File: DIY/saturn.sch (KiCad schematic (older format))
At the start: 7 parts, among them J1 Conn_01x09, J2 Conn_01x09, J3 DB25_Male, U1 74AHCT125N, U2 74AHCT125N, U3 74AHCT125N, U4 74AHCT125N

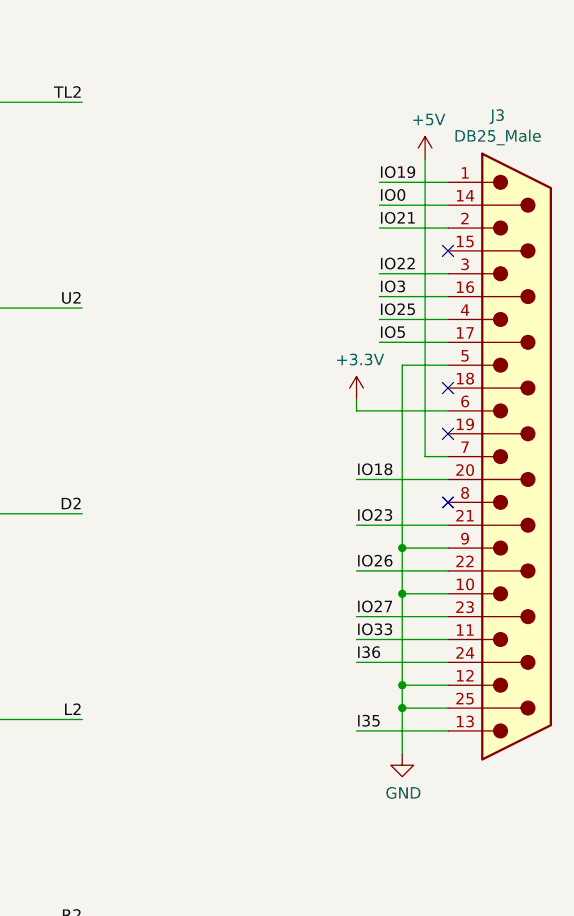
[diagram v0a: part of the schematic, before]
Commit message: [DIY] Update DIY & cable adapter schematic base on new DB25 mapping
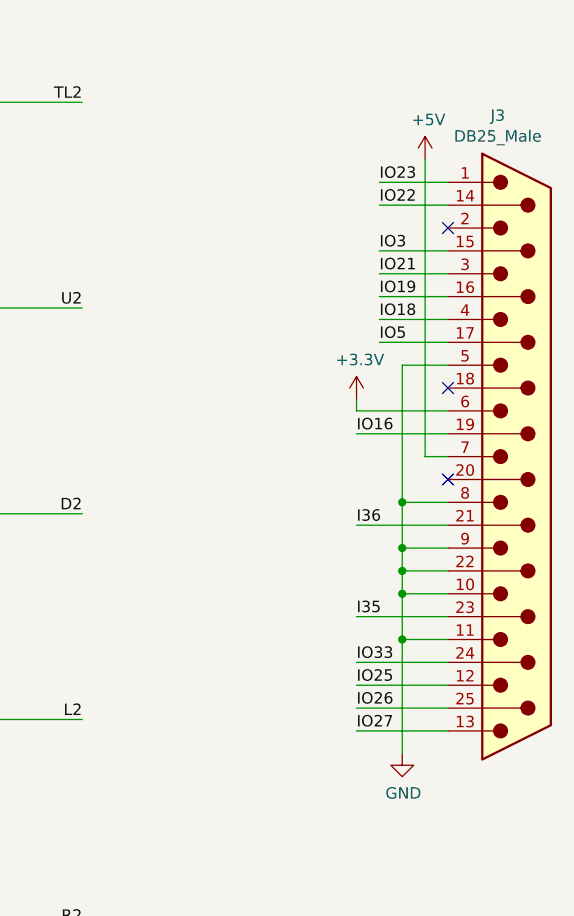
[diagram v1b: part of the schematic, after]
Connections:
- net GND: now also J3.11, J3.22 (P22), J3.8; no longer J3.12, J3.25 (P25)
- net I35: now also J3.23 (P23); no longer J3.13
- net I36: now also J3.21 (P21); no longer J3.24 (P24)
- net IO0: no longer J3.14 (P14)
- net IO18: now also J3.4; no longer J3.20 (P20)
- net IO19: now also J3.16 (P16); no longer J3.1
- net IO21: now also J3.3; no longer J3.2
- net IO22: now also J3.14 (P14); no longer J3.3
- net IO23: now also J3.1; no longer J3.21 (P21)
- net IO25: now also J3.12; no longer J3.4
- net IO26: now also J3.25 (P25); no longer J3.22 (P22)
- net IO27: now also J3.13; no longer J3.23 (P23)
- net IO3: now also J3.15 (P15); no longer J3.16 (P16)
- net IO33: now also J3.24 (P24); no longer J3.11
- net IO16: now reaches J3.19 (P19)
- no-connect marks 6 -> 5
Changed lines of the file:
@@
 $Descr USLetter 11000 8500
 encoding utf-8
-Sheet 2 4
+Sheet 2 7
 Title "BlueRetro - Saturn adapter cable"
-Date "2020-07-16"
-Rev "v1.0"
+Date "2020-08-22"
+Rev "v1.1"
 Comp ""
 Comment1 ""
@@
 	9050 1700 9350 1700
 Wire Wire Line
-	9050 1900 9350 1900
-Wire Wire Line
 	9050 2100 9350 2100
 Wire Wire Line
@@
 	9350 2500 9150 2500
 Wire Wire Line
-	9150 2500 9150 3300
+	9150 2500 9150 3100
 Wire Wire Line
 	9350 3300 9150 3300
-Connection ~ 9150 3300
-Wire Wire Line
-	9150 3300 9150 3500
-Wire Wire Line
-	9350 4000 9150 4000
-Connection ~ 9150 4000
-Wire Wire Line
-	9150 4000 9150 4200
 Wire Wire Line
 	9250 1600 9250 2900
@@
 Text Label 1400 4350 2    50   ~ 0
 L2
-Text Label 9050 1700 0    50   ~ 0
+Text Label 9050 2200 0    50   ~ 0
 IO19
-Text Label 9050 1900 0    50   ~ 0
+Text Label 9050 2100 0    50   ~ 0
 IO21
-Text Label 9050 2100 0    50   ~ 0
+Text Label 9050 1800 0    50   ~ 0
 IO22
-Text Label 9050 2300 0    50   ~ 0
+Text Label 8950 3900 0    50   ~ 0
 IO25
 Wire Wire Line
@@
 	8950 2700 9350 2700
 Wire Wire Line
-	9350 3700 8950 3700
-Wire Wire Line
-	8950 3000 9350 3000
-Wire Wire Line
 	9350 4100 8950 4100
 Wire Wire Line
@@
 	9350 3600 8950 3600
 Wire Wire Line
-	9350 3400 8950 3400
-Wire Wire Line
 	9350 3200 8950 3200
-NoConn ~ 9350 2000
-NoConn ~ 9350 2600
-NoConn ~ 9350 2800
-NoConn ~ 9350 3100
-Text Label 9050 1800 0    50   ~ 0
-IO0
-Text Label 9050 2200 0    50   ~ 0
+Text Label 8950 2800 0    50   ~ 0
+IO16
+Text Label 9050 2000 0    50   ~ 0
 IO3
 Text Label 9050 2400 0    50   ~ 0
 IO5
-Text Label 8950 3000 0    50   ~ 0
+Text Label 9050 1700 0    50   ~ 0
+IO23
+Text Label 8950 4000 0    50   ~ 0
+IO26
+Text Label 8950 4100 0    50   ~ 0
+IO27
+Text Label 8950 3800 0    50   ~ 0
+IO33
+Text Label 8950 3200 0    50   ~ 0
+I36
+Text Label 8950 3600 0    50   ~ 0
+I35
+Wire Wire Line
+	9350 3100 9150 3100
+Connection ~ 9150 3100
+Wire Wire Line
+	9150 3100 9150 3300
+Wire Wire Line
+	9150 3300 9150 3400
+Connection ~ 9150 3300
+Wire Wire Line
+	9350 3400 9150 3400
+Connection ~ 9150 3400
+Wire Wire Line
+	9150 3400 9150 3500
+Wire Wire Line
+	9350 2800 8950 2800
+Wire Wire Line
+	9350 2000 9050 2000
+Wire Wire Line
+	9350 3900 8950 3900
+Text Label 9050 2300 0    50   ~ 0
 IO18
-Text Label 8950 3200 0    50   ~ 0
-IO23
-Text Label 8950 3400 0    50   ~ 0
-IO26
-Text Label 8950 3600 0    50   ~ 0
-IO27
-Text Label 8950 3700 0    50   ~ 0
-IO33
-Text Label 8950 3800 0    50   ~ 0
-I36
-Text Label 8950 4100 0    50   ~ 0
-I35
-Wire Wire Line
-	9350 3900 9150 3900
-Connection ~ 9150 3900
-Wire Wire Line
-	9150 3900 9150 4000
+Wire Wire Line
+	8950 4000 9350 4000
+Wire Wire Line
+	9350 3700 9150 3700
+Connection ~ 9150 3700
+Wire Wire Line
+	9150 3700 9150 4200
+NoConn ~ 9350 1900
+NoConn ~ 9350 2600
 Wire Wire Line
 	9350 3500 9150 3500
 Connection ~ 9150 3500
 Wire Wire Line
-	9150 3500 9150 3900
+	9150 3500 9150 3700
+NoConn ~ 9350 3000
 $EndSCHEMATC

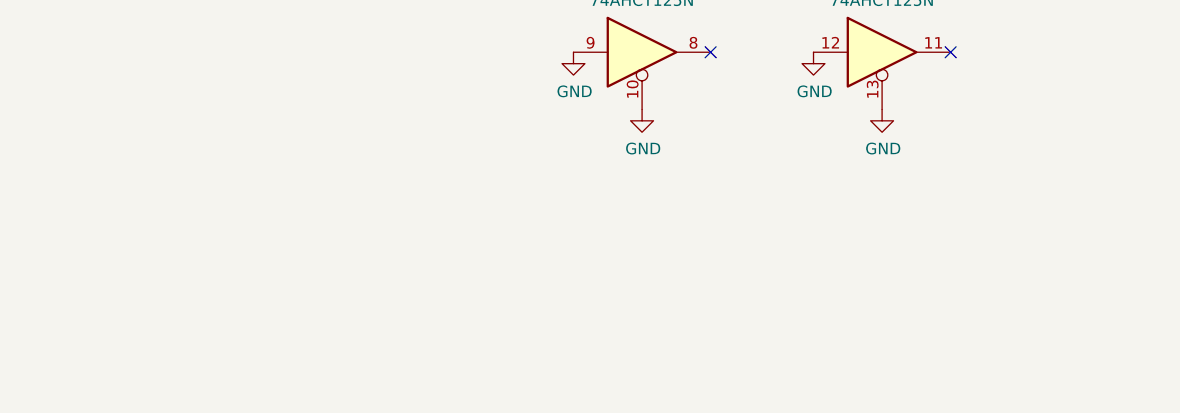
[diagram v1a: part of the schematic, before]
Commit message: [DIY] Add note to cable schematics to underline how important I39 is.
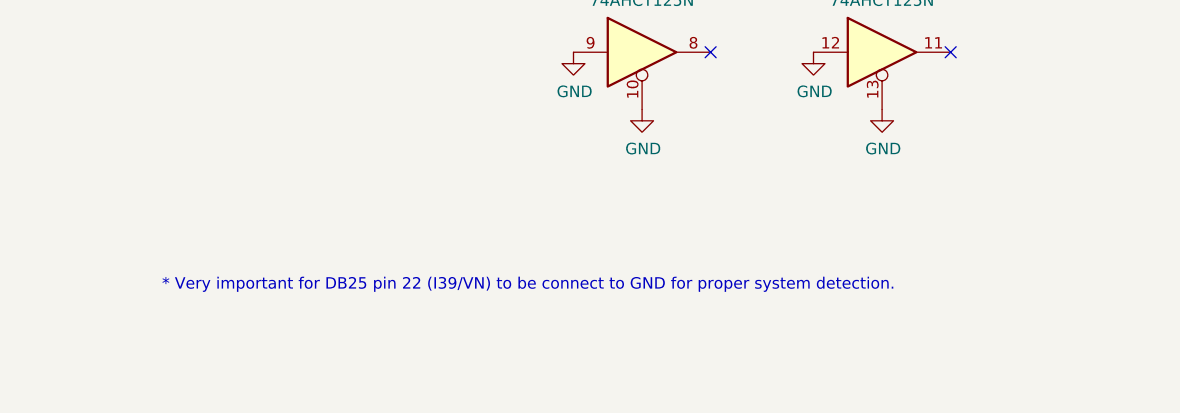
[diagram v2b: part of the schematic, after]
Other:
- note added: "* Very important for DB25 pin 22 (I39/VN) to be connect to GND for proper system detection."
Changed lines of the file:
@@
 	9150 3500 9150 3700
 NoConn ~ 9350 3000
+Text Notes 6350 6900 0    50   ~ 0
+* Very important for DB25 pin 22 (I39/VN) to be connect to GND for proper system detection.
 $EndSCHEMATC

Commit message: Use new port symbol in cable schematic
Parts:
- J1, J2: symbol Connector_Generic:Conn_01x09 -> Connector_Gaming:Saturn
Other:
- note added: "Connectors facing console"
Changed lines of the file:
@@
 Sheet 2 7
 Title "BlueRetro - Saturn adapter cable"
-Date "2020-08-22"
-Rev "v1.1"
-Comp ""
+Date "2020-10-02"
+Rev "v1.2"
+Comp "©2020 Jacques Gagnon, licensed under CC-BY-4.0"
 Comment1 ""
 Comment2 ""
@@
 R2
 $Comp
-L Connector_Generic:Conn_01x09 J1
+L Connector_Gaming:Saturn J1
 U 1 1 5F3ABB96
-P 950 2200
-F 0 "J1" H 868 2817 50  0000 C CNN
-F 1 "Conn_01x09" H 868 2726 50  0000 C CNN
-F 2 "" H 950 2200 50  0001 C CNN
-F 3 "~" H 950 2200 50  0001 C CNN
-	1    950  2200
-	-1   0    0    -1
-$EndComp
-$Comp
-L Connector_Generic:Conn_01x09 J2
-U 1 1 5F3AD383
-P 950 4050
-F 0 "J2" H 868 4667 50  0000 C CNN
-F 1 "Conn_01x09" H 868 4576 50  0000 C CNN
-F 2 "" H 950 4050 50  0001 C CNN
-F 3 "~" H 950 4050 50  0001 C CNN
-	1    950  4050
-	-1   0    0    -1
+P 1600 2950
+F 0 "J1" H 1700 2150 50  0000 C CNN
+F 1 "Conn_01x09" H 1700 2150 50  0001 C CNN
+F 2 "" H 1600 2950 50  0001 C CNN
+F 3 "~" H 1600 2950 50  0001 C CNN
+	1    1600 2950
+	0    1    1    0
 $EndComp
 $Comp
 L power:GND #PWR?
 U 1 1 5F3B346E
-P 1250 2750
-F 0 "#PWR?" H 1250 2500 50  0001 C CNN
-F 1 "GND" H 1255 2577 50  0000 C CNN
-F 2 "" H 1250 2750 50  0001 C CNN
-F 3 "" H 1250 2750 50  0001 C CNN
-	1    1250 2750
-	1    0    0    -1
+P 1950 2650
+F 0 "#PWR?" H 1950 2400 50  0001 C CNN
+F 1 "GND" H 1955 2477 50  0000 C CNN
+F 2 "" H 1950 2650 50  0001 C CNN
+F 3 "" H 1950 2650 50  0001 C CNN
+	1    1950 2650
+	0    -1   -1   0
 $EndComp
 $Comp
 L power:GND #PWR?
 U 1 1 5F3B3833
-P 1250 4600
-F 0 "#PWR?" H 1250 4350 50  0001 C CNN
-F 1 "GND" H 1255 4427 50  0000 C CNN
-F 2 "" H 1250 4600 50  0001 C CNN
-F 3 "" H 1250 4600 50  0001 C CNN
-	1    1250 4600
-	1    0    0    -1
+P 1950 3500
+F 0 "#PWR?" H 1950 3250 50  0001 C CNN
+F 1 "GND" H 1955 3327 50  0000 C CNN
+F 2 "" H 1950 3500 50  0001 C CNN
+F 3 "" H 1950 3500 50  0001 C CNN
+	1    1950 3500
+	0    -1   -1   0
 $EndComp
 $Comp
 L power:+5V #PWR?
 U 1 1 5F3B5AF6
-P 1300 3500
-F 0 "#PWR?" H 1300 3350 50  0001 C CNN
-F 1 "+5V" H 1315 3673 50  0000 C CNN
-F 2 "" H 1300 3500 50  0001 C CNN
-F 3 "" H 1300 3500 50  0001 C CNN
-	1    1300 3500
-	1    0    0    -1
+P 850 3450
+F 0 "#PWR?" H 850 3300 50  0001 C CNN
+F 1 "+5V" H 865 3623 50  0000 C CNN
+F 2 "" H 850 3450 50  0001 C CNN
+F 3 "" H 850 3450 50  0001 C CNN
+	1    850  3450
+	0    -1   -1   0
 $EndComp
 $Comp
 L power:+5V #PWR?
 U 1 1 5F3B6FDE
-P 1300 1650
-F 0 "#PWR?" H 1300 1500 50  0001 C CNN
-F 1 "+5V" H 1315 1823 50  0000 C CNN
-F 2 "" H 1300 1650 50  0001 C CNN
-F 3 "" H 1300 1650 50  0001 C CNN
-	1    1300 1650
-	1    0    0    -1
-$EndComp
-Wire Wire Line
-	1150 1800 1300 1800
-Wire Wire Line
-	1300 1800 1300 1650
-Wire Wire Line
-	1150 2600 1250 2600
-Wire Wire Line
-	1250 2600 1250 2750
-Wire Wire Line
-	1150 3650 1300 3650
-Wire Wire Line
-	1300 3650 1300 3500
-Wire Wire Line
-	1150 4450 1250 4450
-Wire Wire Line
-	1250 4450 1250 4600
-Wire Wire Line
-	1150 4350 1400 4350
-Wire Wire Line
-	1150 4250 1400 4250
-Wire Wire Line
-	1150 4150 1400 4150
-Wire Wire Line
-	1150 4050 1400 4050
-Wire Wire Line
-	1150 3950 1400 3950
-Wire Wire Line
-	1150 3850 1400 3850
-Wire Wire Line
-	1150 3750 1400 3750
-Wire Wire Line
-	1150 2500 1400 2500
-Wire Wire Line
-	1150 2400 1400 2400
-Wire Wire Line
-	1150 2300 1400 2300
-Wire Wire Line
-	1150 2200 1400 2200
-Wire Wire Line
-	1150 2100 1400 2100
-Wire Wire Line
-	1150 2000 1400 2000
-Wire Wire Line
-	1150 1900 1400 1900
-Text Label 1400 1900 2    50   ~ 0
+P 850 2600
+F 0 "#PWR?" H 850 2450 50  0001 C CNN
+F 1 "+5V" H 865 2773 50  0000 C CNN
+F 2 "" H 850 2600 50  0001 C CNN
+F 3 "" H 850 2600 50  0001 C CNN
+	1    850  2600
+	0    -1   -1   0
+$EndComp
+Wire Wire Line
+	1000 2750 1000 2600
+Wire Wire Line
+	1000 2600 850  2600
+Wire Wire Line
+	1800 2750 1800 2650
+Wire Wire Line
+	1800 2650 1950 2650
+Wire Wire Line
+	1000 3600 1000 3450
+Wire Wire Line
+	1000 3450 850  3450
+Wire Wire Line
+	1800 3600 1800 3500
+Wire Wire Line
+	1800 3500 1950 3500
+Wire Wire Line
+	1700 3600 1700 3350
+Wire Wire Line
+	1600 3600 1600 3350
+Wire Wire Line
+	1500 3600 1500 3350
+Wire Wire Line
+	1400 3600 1400 3350
+Wire Wire Line
+	1300 3600 1300 3350
+Wire Wire Line
+	1200 3600 1200 3350
+Wire Wire Line
+	1100 3600 1100 3350
+Wire Wire Line
+	1700 2750 1700 2500
+Wire Wire Line
+	1600 2750 1600 2500
+Wire Wire Line
+	1500 2750 1500 2500
+Wire Wire Line
+	1400 2750 1400 2500
+Wire Wire Line
+	1300 2750 1300 2500
+Wire Wire Line
+	1200 2750 1200 2500
+Wire Wire Line
+	1100 2750 1100 2500
+Text Label 1100 2500 3    50   ~ 0
 D1
-Text Label 1400 2000 2    50   ~ 0
+Text Label 1200 2500 3    50   ~ 0
 U1
-Text Label 1400 2100 2    50   ~ 0
+Text Label 1300 2500 3    50   ~ 0
 TH1
-Text Label 1400 2200 2    50   ~ 0
+Text Label 1400 2500 3    50   ~ 0
 TR1
-Text Label 1400 2300 2    50   ~ 0
+Text Label 1500 2500 3    50   ~ 0
 TL1
-Text Label 1400 2400 2    50   ~ 0
+Text Label 1600 2500 3    50   ~ 0
 R1
-Text Label 1400 2500 2    50   ~ 0
+Text Label 1700 2500 3    50   ~ 0
 L1
-Text Label 1400 3750 2    50   ~ 0
+Text Label 1100 3350 3    50   ~ 0
 D2
-Text Label 1400 3850 2    50   ~ 0
+Text Label 1200 3350 3    50   ~ 0
 U2
-Text Label 1400 3950 2    50   ~ 0
+Text Label 1300 3350 3    50   ~ 0
 TH2
-Text Label 1400 4050 2    50   ~ 0
+Text Label 1400 3350 3    50   ~ 0
 TR2
-Text Label 1400 4150 2    50   ~ 0
+Text Label 1500 3350 3    50   ~ 0
 TL2
-Text Label 1400 4250 2    50   ~ 0
+Text Label 1600 3350 3    50   ~ 0
 R2
-Text Label 1400 4350 2    50   ~ 0
+Text Label 1700 3350 3    50   ~ 0
 L2
 Text Label 9050 2200 0    50   ~ 0
@@
 Text Notes 6350 6900 0    50   ~ 0
 * Very important for DB25 pin 22 (I39/VN) to be connect to GND for proper system detection.
+$Comp
+L Connector_Gaming:Saturn J2
+U 1 1 5F3AD383
+P 1600 3800
+F 0 "J2" H 1700 3000 50  0000 C CNN
+F 1 "Conn_01x09" H 1518 4326 50  0001 C CNN
+F 2 "" H 1600 3800 50  0001 C CNN
+F 3 "~" H 1600 3800 50  0001 C CNN
+	1    1600 3800
+	0    1    1    0
+$EndComp
+Text Notes 950  3250 0    50   ~ 0
+Connectors facing console
 $EndSCHEMATC
